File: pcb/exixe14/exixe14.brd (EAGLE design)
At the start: 20 x 40 mm, 50 parts, among them IC1 STM32F042K6

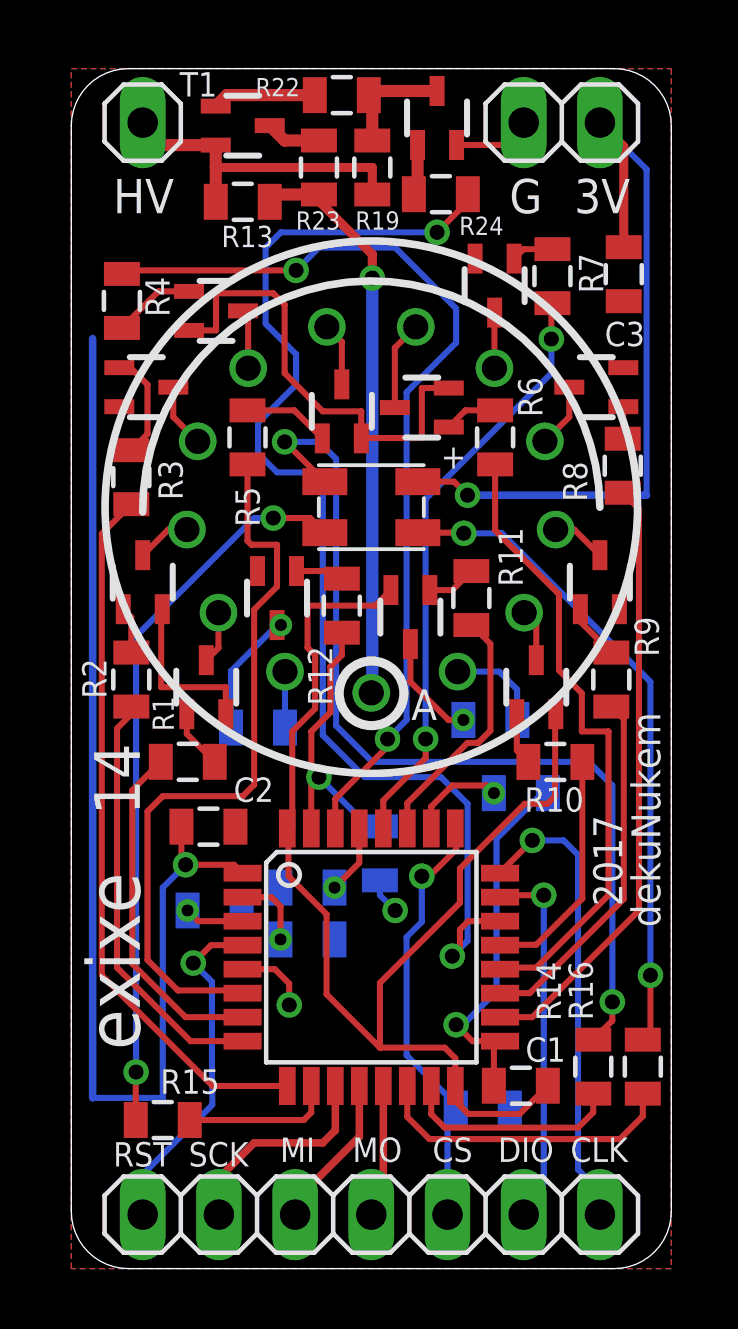
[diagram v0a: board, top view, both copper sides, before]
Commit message: removed DP resistor, new pogo firmware
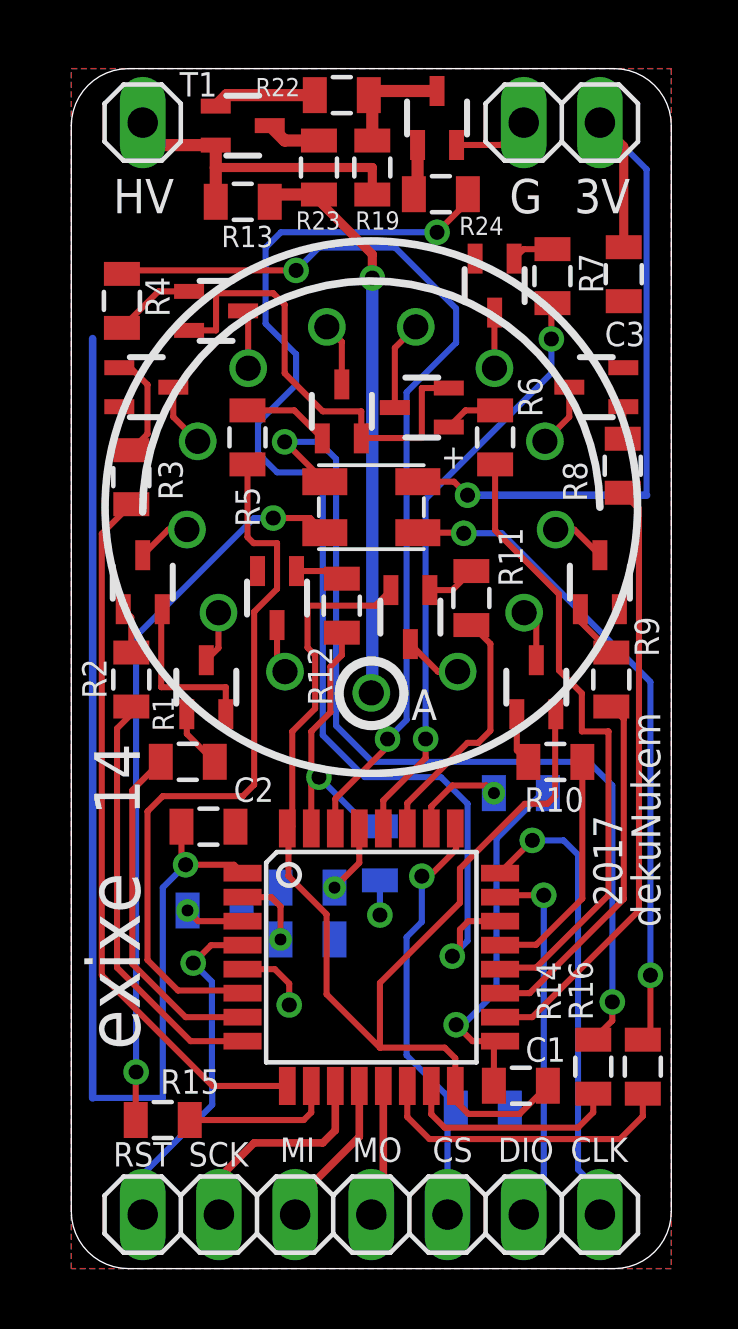
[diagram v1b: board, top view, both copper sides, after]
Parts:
- removed R20, R21: 10K, joyAnalog:0805
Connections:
- removed net N$17: Q12.3, R21.1
- removed net N$18: Q11.3, R20.1
- net NIXIE_DOT_LEFT: now also Q11.3; no longer R20.2
- net NIXIE_DOT_RIGHT: now also Q12.3; no longer R21.2
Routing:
- net N$17: track 4.31 -> 0.00 mm, vias 1 -> 0
- net N$18: track 3.55 -> 0.00 mm, vias 1 -> 0
- net NIXIE_DOT_LEFT: track 3.25 -> 1.95 mm
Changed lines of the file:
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@@
 <setting verticaltext="up"/>
 </settings>
-<grid distance="2" unitdist="mil" unit="mil" style="lines" multiple="1" display="no" altdistance="1" altunitdist="mil" altunit="mil"/>
+<grid distance="1" unitdist="mil" unit="mil" style="lines" multiple="1" display="no" altdistance="1" altunitdist="mil" altunit="mil"/>
 <layers>
 <layer number="1" name="Top" color="4" fill="1" visible="yes" active="yes"/>
@@
 <attribute name="NAME" x="10.9474" y="35.2425" size="0.6096" layer="25" rot="R180"/>
 </element>
-<element name="R20" library="joyAnalog" package="0805" value="10K" x="13.97" y="18.288" smashed="yes" rot="MR180">
-<attribute name="NAME" x="15.494" y="18.6309" size="0.8128" layer="26" rot="MR180"/>
-</element>
-<element name="R21" library="joyAnalog" package="0805" value="10K" x="6.223" y="18.034" smashed="yes" rot="MR180">
-<attribute name="NAME" x="5.1054" y="17.0053" size="0.8128" layer="26" rot="MR180"/>
-</element>
 <element name="R25" library="joyAnalog" package="0805" value="10K" x="10.287" y="13.843" smashed="yes" rot="MR90">
 <attribute name="NAME" x="11.4173" y="13.9954" size="0.8128" layer="26" rot="MR90"/>
@@
 <wire x1="14.334" y1="37.454" x2="15.08" y2="38.2" width="0.2032" layer="1"/>
 <contactref element="R25" pad="1"/>
-<via x="10.795" y="11.938" extent="1-16" drill="0.5"/>
-<wire x1="10.287" y1="12.943" x2="10.287" y2="12.446" width="0.2032" layer="16"/>
-<wire x1="10.287" y1="12.446" x2="10.795" y2="11.938" width="0.2032" layer="16"/>
+<via x="10.287" y="11.7856" extent="1-16" drill="0.5"/>
+<wire x1="10.287" y1="12.943" x2="10.287" y2="11.7856" width="0.2032" layer="16"/>
 <wire x1="15.875" y1="15.494" x2="15.113" y2="15.494" width="0.2032" layer="1"/>
 <wire x1="15.113" y1="15.494" x2="12.954" y2="13.335" width="0.2032" layer="1"/>
@@
 <signal name="NIXIE_DOT_LEFT">
 <contactref element="N1" pad="LHDP"/>
-<contactref element="R20" pad="2"/>
-<wire x1="12.8766" y1="19.9001" x2="14.2629" y2="19.9001" width="0.2032" layer="16"/>
-<wire x1="14.2629" y1="19.9001" x2="14.859" y2="19.304" width="0.2032" layer="16"/>
-<wire x1="14.859" y1="19.304" x2="14.859" y2="18.299" width="0.2032" layer="16"/>
-<wire x1="14.859" y1="18.299" x2="14.87" y2="18.288" width="0.2032" layer="16"/>
+<contactref element="Q11" pad="3"/>
+<wire x1="11.303" y1="20.817" x2="12.2199" y2="19.9001" width="0.2032" layer="1"/>
+<wire x1="12.2199" y1="19.9001" x2="12.8766" y2="19.9001" width="0.2032" layer="1"/>
 </signal>
 <signal name="NIXIE_DOT_RIGHT">
 <contactref element="N1" pad="RHDP"/>
-<contactref element="R21" pad="2"/>
-<wire x1="7.123" y1="18.034" x2="7.123" y2="19.8997" width="0.2032" layer="16"/>
-<wire x1="7.123" y1="19.8997" x2="7.1234" y2="19.9001" width="0.2032" layer="16"/>
+<contactref element="Q12" pad="3"/>
+<wire x1="6.858" y1="21.452" x2="6.858" y2="20.1655" width="0.2032" layer="1"/>
+<wire x1="6.858" y1="20.1655" x2="7.1234" y2="19.9001" width="0.2032" layer="1"/>
 </signal>
 <signal name="+3V3">
@@
 <contactref element="R5" pad="1"/>
 <contactref element="IC1" pad="6"/>
-<wire x1="6.096" y1="21.971" x2="6.858" y2="22.733" width="0.2032" layer="1"/>
+<wire x1="6.096" y1="21.8948" x2="6.858" y2="22.6568" width="0.2032" layer="1"/>
 <wire x1="2.54" y1="15.24" x2="3.048" y2="15.748" width="0.2032" layer="1"/>
 <wire x1="2.54" y1="15.24" x2="2.54" y2="10.287" width="0.2032" layer="1"/>
@@
 <wire x1="3.556" y1="9.271" x2="5.6174" y2="9.271" width="0.2032" layer="1"/>
 <wire x1="5.6174" y1="9.271" x2="5.7074" y2="9.181" width="0.2032" layer="1"/>
-<wire x1="6" y1="24.13" x2="6.858" y2="24.13" width="0.2032" layer="1"/>
-<wire x1="6.858" y1="24.13" x2="6.858" y2="22.733" width="0.2032" layer="1"/>
-<wire x1="5.873" y1="26.808" x2="5.873" y2="24.257" width="0.2032" layer="1"/>
-<wire x1="5.873" y1="24.257" x2="6" y2="24.13" width="0.2032" layer="1"/>
+<wire x1="6.0762" y1="24.1808" x2="6.858" y2="24.1808" width="0.2032" layer="1"/>
+<wire x1="6.858" y1="24.1808" x2="6.858" y2="22.6568" width="0.2032" layer="1"/>
+<wire x1="5.873" y1="26.808" x2="5.873" y2="24.384" width="0.2032" layer="1"/>
+<wire x1="5.873" y1="24.384" x2="6.0762" y2="24.1808" width="0.2032" layer="1"/>
 <wire x1="3.048" y1="15.748" x2="5.715" y2="15.748" width="0.2032" layer="1"/>
 <wire x1="5.715" y1="15.748" x2="6.096" y2="16.129" width="0.2032" layer="1"/>
-<wire x1="6.096" y1="16.129" x2="6.096" y2="21.971" width="0.2032" layer="1"/>
+<wire x1="6.096" y1="16.129" x2="6.096" y2="21.8948" width="0.2032" layer="1"/>
 </signal>
 <signal name="STM_4">
@@
 <wire x1="13.219" y1="35.571" x2="12.192" y2="34.544" width="0.2032" layer="1"/>
 </signal>
-<signal name="N$17">
-<contactref element="Q12" pad="3"/>
-<contactref element="R21" pad="1"/>
-<via x="6.985" y="21.452" extent="1-16" drill="0.4"/>
-<wire x1="5.323" y1="18.034" x2="5.323" y2="19.917" width="0.2032" layer="16"/>
-<wire x1="6.858" y1="21.452" x2="6.985" y2="21.452" width="0.2032" layer="1"/>
-<wire x1="5.323" y1="19.917" x2="6.858" y2="21.452" width="0.2032" layer="16"/>
-<wire x1="6.858" y1="21.452" x2="6.985" y2="21.452" width="0.2032" layer="16"/>
-</signal>
-<signal name="N$18">
-<contactref element="Q11" pad="3"/>
-<contactref element="R20" pad="1"/>
-<via x="13.07" y="18.288" extent="1-16" drill="0.4"/>
-<wire x1="11.303" y1="20.817" x2="11.303" y2="19.558" width="0.2032" layer="1"/>
-<wire x1="12.573" y1="18.288" x2="13.07" y2="18.288" width="0.2032" layer="1"/>
-<wire x1="11.303" y1="19.558" x2="12.573" y2="18.288" width="0.2032" layer="1"/>
-</signal>
 <signal name="N$25">

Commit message: cleanup
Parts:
- removed R18: 10K, joyAnalog:0805
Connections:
- net +3V3: no longer R18.2
- net SPI_CS: no longer R18.1
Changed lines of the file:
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@@
 <attribute name="NAME" x="17.3863" y="8.2804" size="0.8128" layer="25" font="vector" rot="R90"/>
-</element>
-<element name="R18" library="joyAnalog" package="0805" value="10K" x="13.716" y="5.334" smashed="yes" rot="MR180">
-<attribute name="NAME" x="12.5222" y="7.0485" size="0.8128" layer="26" font="vector" rot="MR180"/>
 </element>
 <element name="R22" library="joyAnalog" package="0805" value="1M" x="9.017" y="39.116" smashed="yes">
@@
 <wire x1="14.086" y1="7.3744" x2="14.086" y2="6.096" width="0.2032" layer="1"/>
 <wire x1="3.683" y1="14.721" x2="3.672" y2="14.732" width="0.2032" layer="1"/>
-<contactref element="R18" pad="2"/>
 <wire x1="5.7074" y1="13.181" x2="5.4264" y2="13.462" width="0.2032" layer="1"/>
 <wire x1="5.4264" y1="13.462" x2="3.81" y2="13.462" width="0.2032" layer="1"/>
@@
 <signal name="SPI_CS">
 <contactref element="JP2" pad="5"/>
-<contactref element="R18" pad="1"/>
-<wire x1="12.54" y1="1.8" x2="12.54" y2="5.058" width="0.2032" layer="16"/>
-<wire x1="12.816" y1="5.334" x2="12.54" y2="5.058" width="0.2032" layer="16"/>
 <contactref element="IC1" pad="25"/>
 <via x="11.684" y="13.081" extent="1-16" drill="0.5"/>
@@
 <wire x1="11.684" y1="11.557" x2="11.176" y2="11.049" width="0.2032" layer="16"/>
 <wire x1="11.176" y1="11.049" x2="11.176" y2="7.112" width="0.2032" layer="16"/>
-<wire x1="11.176" y1="7.112" x2="12.816" y2="5.472" width="0.2032" layer="16"/>
-<wire x1="12.816" y1="5.472" x2="12.816" y2="5.334" width="0.2032" layer="16"/>
+<wire x1="11.176" y1="7.112" x2="12.54" y2="5.748" width="0.2032" layer="16"/>
+<wire x1="12.54" y1="5.748" x2="12.54" y2="1.8" width="0.2032" layer="16"/>
 </signal>
 <signal name="SWD_DIO">

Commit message: prepare for a new production run
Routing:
- net +3V3: track 79.4 -> 100.6 mm
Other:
- board text added: "PD4 SEPT19"
- board text removed: "NOV18"
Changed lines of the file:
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@@
 <grid distance="1" unitdist="mil" unit="mil" style="lines" multiple="1" display="no" altdistance="1" altunitdist="mil" altunit="mil"/>
 <layers>
-<layer number="1" name="Top" color="4" fill="1" visible="yes" active="yes"/>
+<layer number="1" name="Top" color="4" fill="1" visible="no" active="yes"/>
 <layer number="2" name="Route2" color="1" fill="3" visible="no" active="yes"/>
 <layer number="3" name="Route3" color="4" fill="3" visible="no" active="yes"/>
@@
 <layer number="19" name="Unrouted" color="6" fill="1" visible="yes" active="yes"/>
 <layer number="20" name="Dimension" color="15" fill="1" visible="yes" active="yes"/>
-<layer number="21" name="tPlace" color="7" fill="1" visible="yes" active="yes"/>
+<layer number="21" name="tPlace" color="7" fill="1" visible="no" active="yes"/>
 <layer number="22" name="bPlace" color="7" fill="1" visible="yes" active="yes"/>
-<layer number="23" name="tOrigins" color="15" fill="1" visible="yes" active="yes"/>
+<layer number="23" name="tOrigins" color="15" fill="1" visible="no" active="yes"/>
 <layer number="24" name="bOrigins" color="15" fill="1" visible="yes" active="yes"/>
-<layer number="25" name="tNames" color="7" fill="1" visible="yes" active="yes"/>
+<layer number="25" name="tNames" color="7" fill="1" visible="no" active="yes"/>
 <layer number="26" name="bNames" color="7" fill="1" visible="yes" active="yes"/>
-<layer number="27" name="tValues" color="7" fill="1" visible="yes" active="yes"/>
-<layer number="28" name="bValues" color="7" fill="1" visible="yes" active="yes"/>
+<layer number="27" name="tValues" color="7" fill="1" visible="no" active="yes"/>
+<layer number="28" name="bValues" color="7" fill="1" visible="no" active="yes"/>
 <layer number="29" name="tStop" color="7" fill="3" visible="no" active="yes"/>
 <layer number="30" name="bStop" color="7" fill="6" visible="no" active="yes"/>
@@
 <layer number="38" name="bTest" color="7" fill="1" visible="no" active="yes"/>
 <layer number="39" name="tKeepout" color="4" fill="11" visible="no" active="yes"/>
-<layer number="40" name="bKeepout" color="1" fill="11" visible="no" active="yes"/>
-<layer number="41" name="tRestrict" color="4" fill="10" visible="yes" active="yes"/>
-<layer number="42" name="bRestrict" color="1" fill="10" visible="no" active="yes"/>
+<layer number="40" name="bKeepout" color="1" fill="11" visible="yes" active="yes"/>
+<layer number="41" name="tRestrict" color="4" fill="10" visible="no" active="yes"/>
+<layer number="42" name="bRestrict" color="1" fill="10" visible="yes" active="yes"/>
 <layer number="43" name="vRestrict" color="2" fill="10" visible="no" active="yes"/>
 <layer number="44" name="Drills" color="7" fill="1" visible="no" active="yes"/>
@@
 <layer number="49" name="Reference" color="7" fill="1" visible="no" active="yes"/>
 <layer number="50" name="dxf" color="7" fill="1" visible="no" active="yes"/>
-<layer number="51" name="tDocu" color="7" fill="1" visible="yes" active="yes"/>
+<layer number="51" name="tDocu" color="7" fill="1" visible="no" active="yes"/>
 <layer number="52" name="bDocu" color="7" fill="1" visible="yes" active="yes"/>
 <layer number="53" name="tGND_GNDA" color="7" fill="1" visible="no" active="yes"/>
@@
 <vertex x="8.3312" y="35.4076"/>
 </polygon>
-<text x="1.778" y="35.56" size="1.016" layer="26" font="vector" rot="MR270">NOV18</text>
+<text x="1.778" y="35.56" size="1.016" layer="26" font="vector" rot="MR270">PD4 SEPT19</text>
 </plain>
 <attributes>
@@
 <wire x1="14.2926" y1="7.581" x2="14.086" y2="7.3744" width="0.2032" layer="1"/>
 <wire x1="14.086" y1="7.3744" x2="14.086" y2="6.096" width="0.2032" layer="1"/>
-<wire x1="3.683" y1="14.721" x2="3.672" y2="14.732" width="0.2032" layer="1"/>
 <wire x1="5.7074" y1="13.181" x2="5.4264" y2="13.462" width="0.2032" layer="1"/>
 <wire x1="5.4264" y1="13.462" x2="3.81" y2="13.462" width="0.2032" layer="1"/>
@@
 <wire x1="7.2644" y1="9.4996" x2="7.2644" y2="8.7884" width="0.2032" layer="1"/>
 <wire x1="3.81" y1="13.462" x2="3.048" y2="12.7" width="0.2032" layer="16"/>
-<wire x1="3.048" y1="12.7" x2="3.048" y2="5.6896" width="0.2032" layer="16"/>
-<wire x1="3.048" y1="5.6896" x2="0.7112" y2="5.6896" width="0.2032" layer="16"/>
+<wire x1="3.048" y1="5.6896" x2="3.048" y2="12.7" width="0.2032" layer="16"/>
 <wire x1="14.2926" y1="7.581" x2="13.374" y2="7.581" width="0.2032" layer="1"/>
 <wire x1="13.374" y1="7.581" x2="12.827" y2="8.128" width="0.2032" layer="1"/>
 <wire x1="13.208" y1="25.781" x2="19.177" y2="25.781" width="0.254" layer="16"/>
-<wire x1="0.7112" y1="5.6896" x2="0.7112" y2="31.0012" width="0.254" layer="16"/>
 <contactref element="JP1" pad="7"/>
 <wire x1="18.415" y1="37.405" x2="17.62" y2="38.2" width="0.3048" layer="1"/>
@@
 <wire x1="15.6972" y1="15.8496" x2="14.1732" y2="14.3256" width="0.2032" layer="16"/>
 <wire x1="14.1732" y1="14.3256" x2="14.1732" y2="9.2456" width="0.2032" layer="16"/>
+<wire x1="0.7112" y1="31.0012" x2="0.7112" y2="31.0012" width="0.254" layer="16"/>
+<wire x1="0.7112" y1="31.0012" x2="5.397" y2="35.687" width="0.254" layer="16"/>
+<wire x1="16.2306" y1="35.687" x2="5.397" y2="35.687" width="0.254" layer="16"/>
+<wire x1="17.62" y1="38.2" x2="17.62" y2="37.0764" width="0.254" layer="16"/>
+<wire x1="17.62" y1="37.0764" x2="16.2306" y2="35.687" width="0.254" layer="16"/>
+<wire x1="0.7112" y1="31.0012" x2="0.7112" y2="5.8674" width="0.254" layer="16"/>
+<wire x1="0.7112" y1="5.8674" x2="1.7526" y2="4.826" width="0.254" layer="16"/>
+<wire x1="1.7526" y1="4.826" x2="2.1844" y2="4.826" width="0.254" layer="16"/>
+<wire x1="2.1844" y1="4.826" x2="3.048" y2="5.6896" width="0.254" layer="16"/>
 </signal>
 <signal name="SPI_SCK">
@@
 <wire x1="8.636" y1="20.066" x2="8.636" y2="18.542" width="0.2032" layer="1"/>
 <wire x1="8.636" y1="18.542" x2="8.001" y2="17.907" width="0.2032" layer="1"/>
-<wire x1="8.001" y1="14.6746" x2="8" y2="14.6736" width="0.2032" layer="1"/>
 <contactref element="R25" pad="2"/>
 <via x="8.255" y="16.383" extent="1-16" drill="0.5"/>
@@
 <contactref element="Q13" pad="3"/>
 <contactref element="R19" pad="2"/>
-<wire x1="9.917" y1="39.127" x2="9.917" y2="39.116" width="0.3048" layer="1"/>
 <wire x1="9.917" y1="39.116" x2="10.033" y2="39" width="0.4064" layer="1"/>
 <wire x1="10.033" y1="39" x2="10.033" y2="37.603" width="0.4064" layer="1"/>
